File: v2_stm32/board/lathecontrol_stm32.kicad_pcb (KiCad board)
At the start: 2 copper layers, 99 x 79 mm, 81 parts, among them IC1 LM393, IC2 LM393, IC3 LM393, IC4 LM393, J1 Conn_01x06_Male, J10 USB_A, J11 USB_A, J12 USB_A, J13 Conn_01x04_Male, J3 Barrel_Jack_Switch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

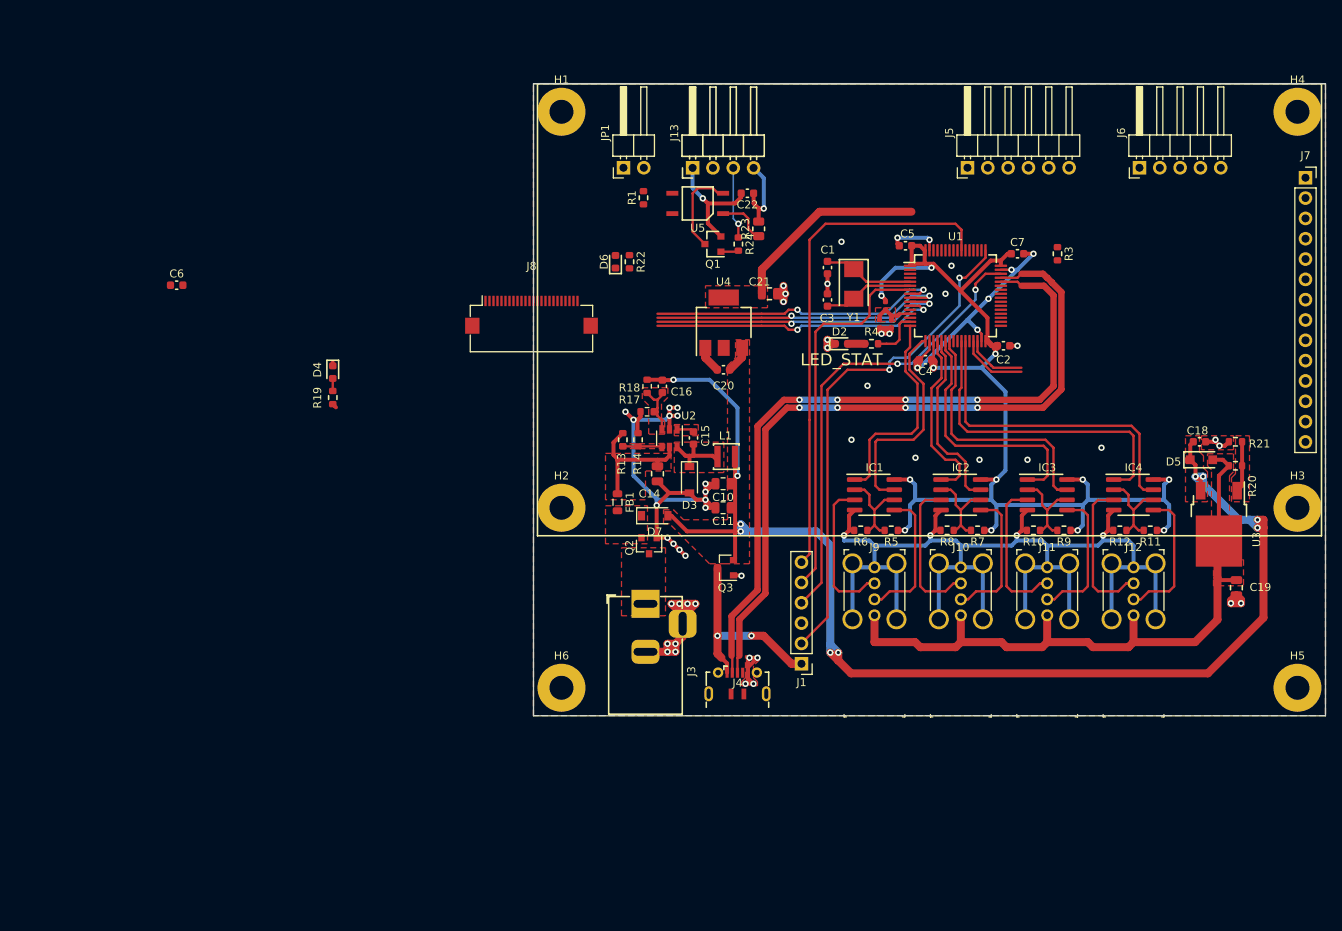
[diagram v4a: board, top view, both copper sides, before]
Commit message: Moved to 4 layer PCB. More routing
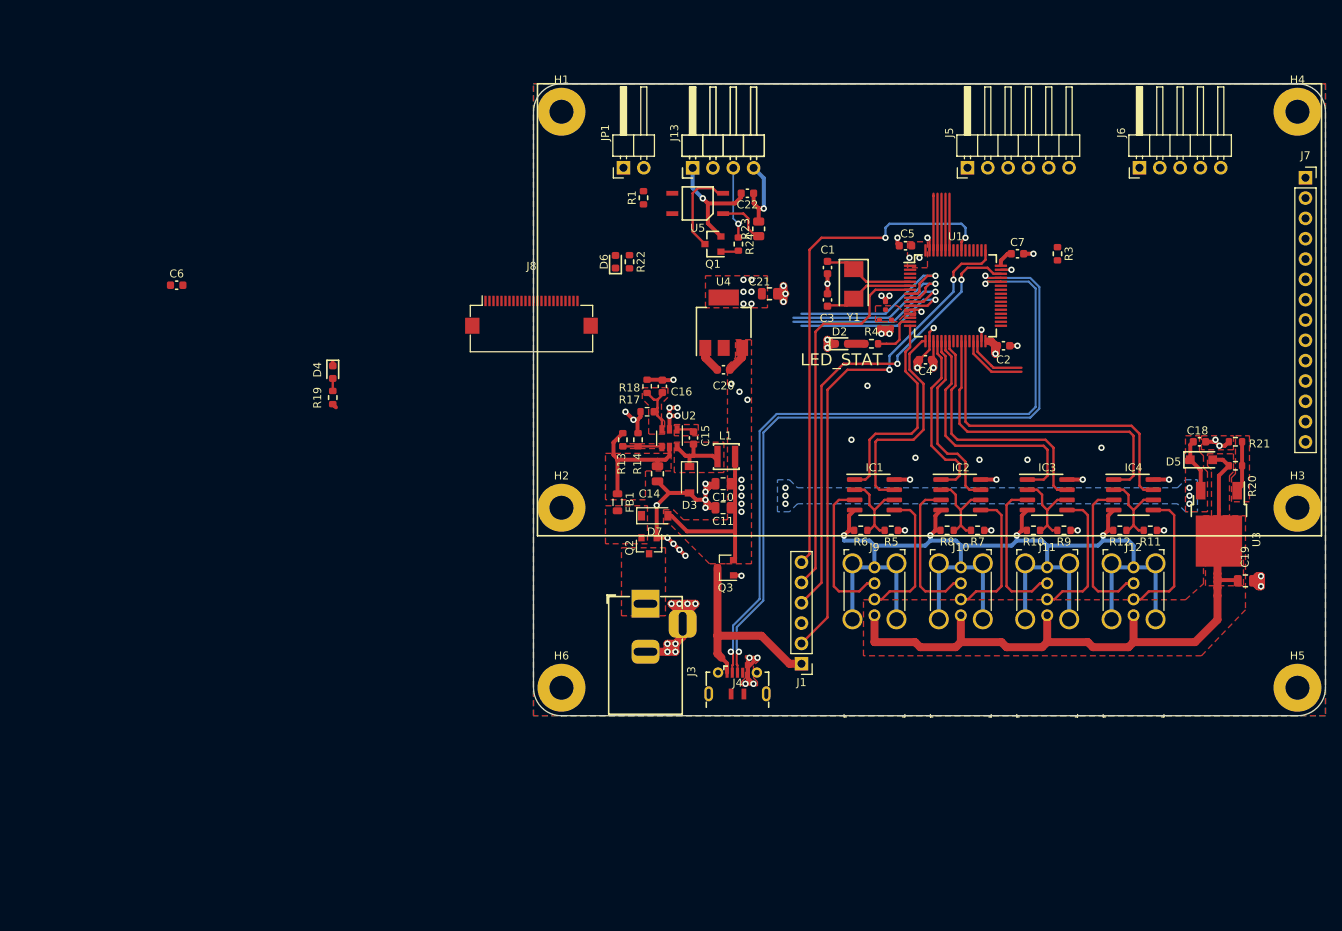
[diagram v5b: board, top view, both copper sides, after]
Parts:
- moved C19 1.41 mm to (222.5, 129.6), turned to 0 degrees
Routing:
- net +3V3: track 165.8 -> 21.7 mm, vias 12 -> 20
- net +5V: track 175.3 -> 37.7 mm, vias 10 -> 15
- net GND: track 308.0 -> 262.1 mm, vias 62 -> 60
- net ADC4: track 36.4 -> 21.3 mm, vias 2 -> 1
- net ADC3: track 37.7 -> 23.0 mm, vias 2 -> 1
- net ADC2: track 37.9 -> 23.7 mm, vias 2 -> 1
- net ADC1: track 36.8 -> 23.4 mm, vias 2 -> 1
- net UART_TX: track 0.00 -> 7.08 mm
- net UART_RX: track 0.00 -> 7.08 mm
- net I2C_SDA: track 0.00 -> 7.08 mm
- net I2C_SCL: track 0.00 -> 7.08 mm
- net /BOOT0: track 0.00 -> 7.08 mm
- net +3.3VA: track 5.60 -> 0.00 mm
- net SWDIO: track 57.6 -> 58.9 mm
- net USB_D-: track 90.0 -> 91.3 mm, vias 4 -> 2
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- added copper zone on In1.Cu, net +3V3
- added copper zone on B.Cu, net +5V
- added copper zone on In1.Cu, net +5V
- added copper zone on In2.Cu, net GND
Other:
- outline, holes or cut-outs redrawn
- copper layers 2 -> 4

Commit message: Started current loop output for frequency converter
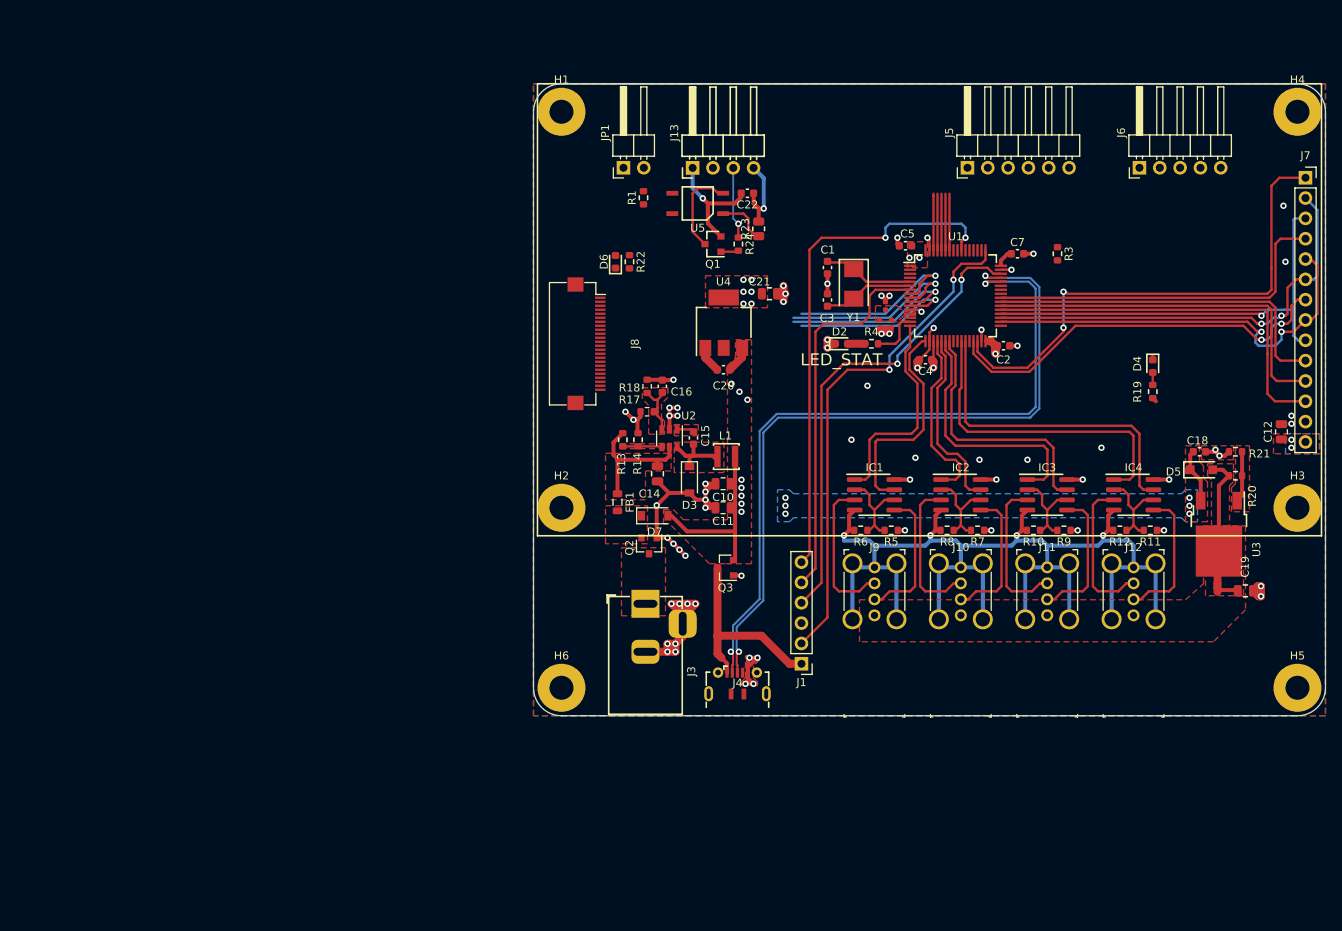
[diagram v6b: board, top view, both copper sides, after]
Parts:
- removed the C7 at (194.0, 88.8)
- added C12: 10u, Capacitor_SMD:C_0805_2012Metric, F.Cu at (227.0, 111.0)
- H1, H2, H3, H4, H5, H6: value MountingHole_Pad -> MH3mm
- moved C7 105.2 mm to (194.0, 88.8)
- moved D4 102.5 mm to (210.9, 102.8)
- moved R19 102.5 mm to (210.9, 106.0)
- moved J8 11.0 mm to (142.5, 100.0), turned to 270 degrees
- moved C18 1.25 mm to (216.8, 113.5)
- moved C19 1.25 mm to (222.5, 130.9)
- moved D5 1.25 mm to (217.0, 115.8)
- moved R20 1.25 mm to (221.2, 116.5)
- moved R21 1.25 mm to (221.2, 113.5)
- moved U3 1.25 mm to (219.2, 123.8)
- renumbered C6 to C7
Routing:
- net +1V8: track 85.9 -> 22.1 mm
- net DISPL_T_IRQ: track 7.65 -> 63.7 mm, vias 0 -> 2
- net DISPL_MOSI: track 0.00 -> 54.8 mm, vias 0 -> 1
- net DISPL_MISO: track 0.00 -> 54.6 mm, vias 0 -> 2
- net DISPL_SCK: track 0.00 -> 53.4 mm, vias 0 -> 2
- net DISPL_CS: track 0.00 -> 48.8 mm
- net DISPL_RST: track 0.00 -> 46.8 mm
- net DISPL_T_CS: track 0.00 -> 44.6 mm
- net DISPL_DC: track 0.00 -> 44.6 mm
- net DISPL_LED: track 8.51 -> 50.8 mm, vias 0 -> 2
- net GND: vias 60 -> 64
- net +5V: vias 15 -> 17

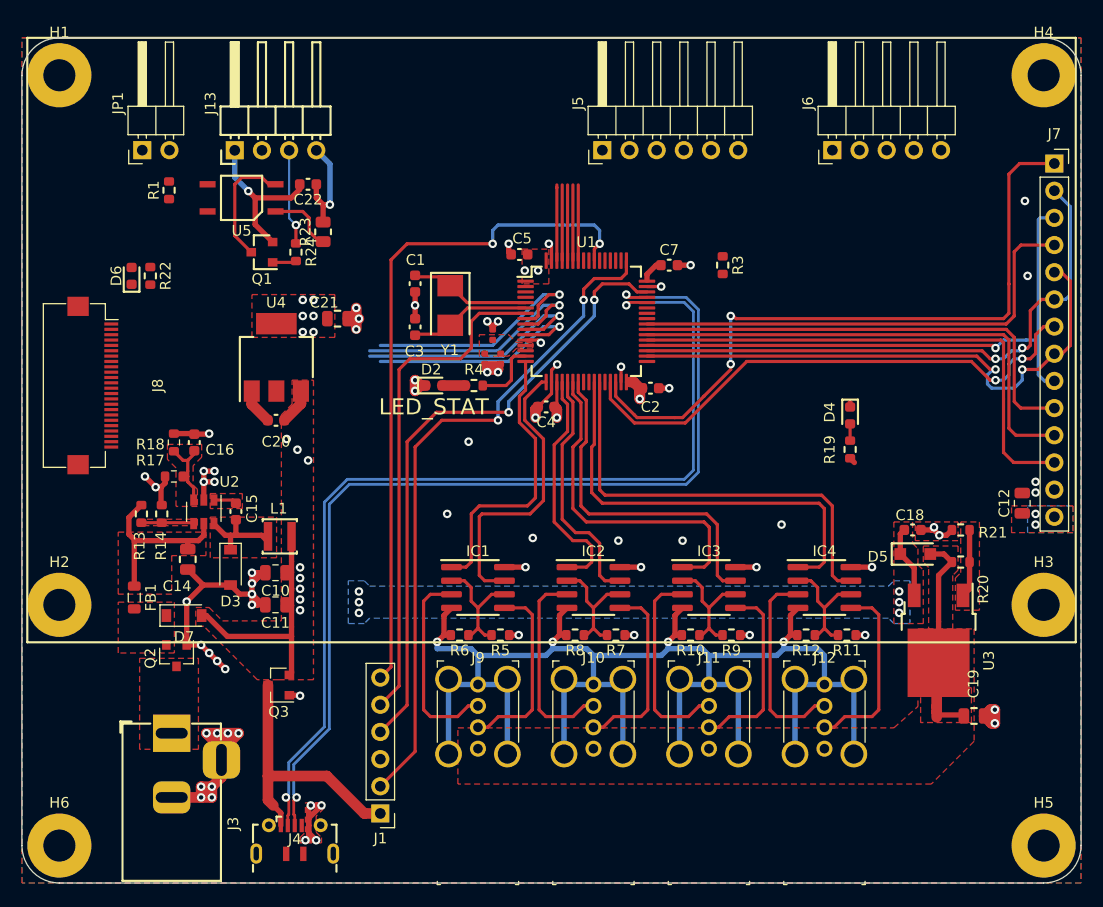
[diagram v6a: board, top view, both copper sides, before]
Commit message: Migrate to Kicad 6
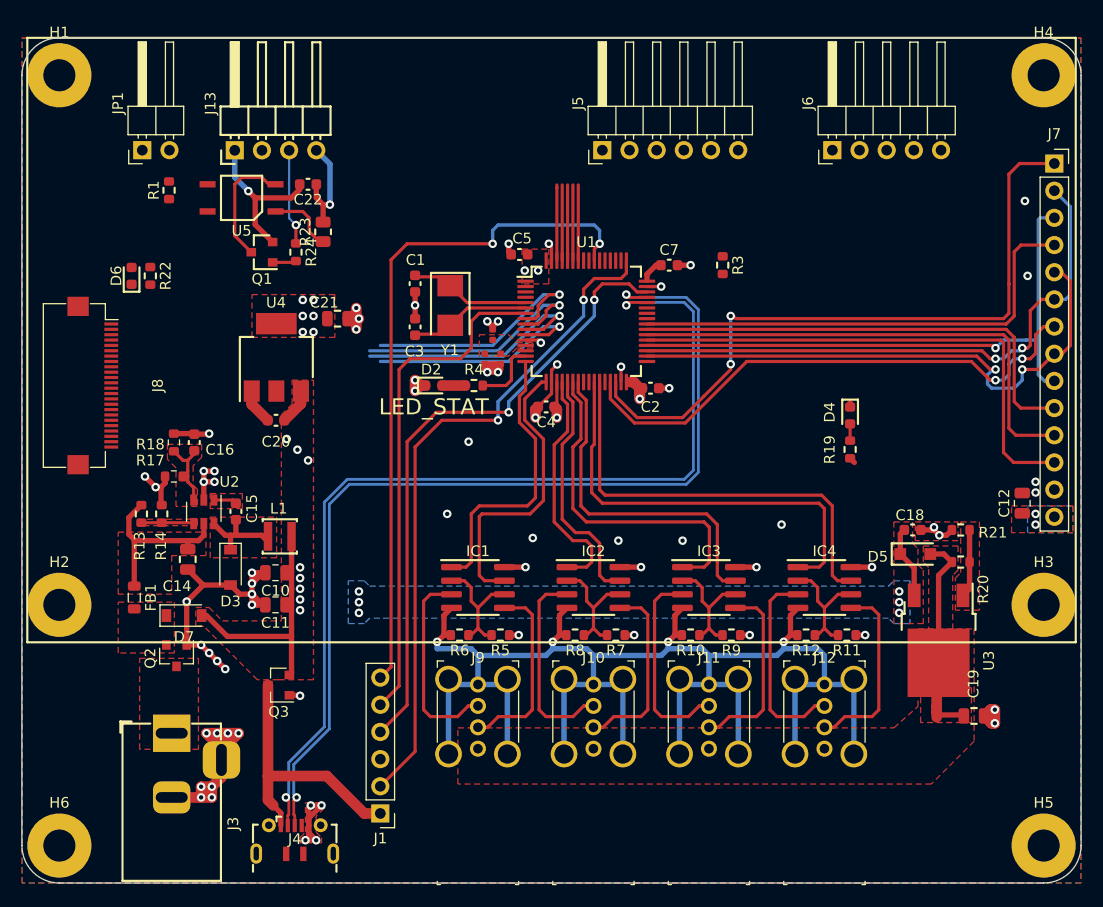
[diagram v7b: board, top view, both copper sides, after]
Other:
- net class Default removed
- net class Power removed
- net class USB removed
